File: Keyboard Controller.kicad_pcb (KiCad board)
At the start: 2 copper layers, 76.2 x 101.6 mm, 48 parts, among them SW1 SW_Push, SW2 SW_Push, SW3 SW_Push, SW4 SW_Push, SW5 SW_Push, SW6 SW_Push, SW7 SW_Push, SW8 SW_Push, SW9 SW_Push, U1 Teensy-3.2

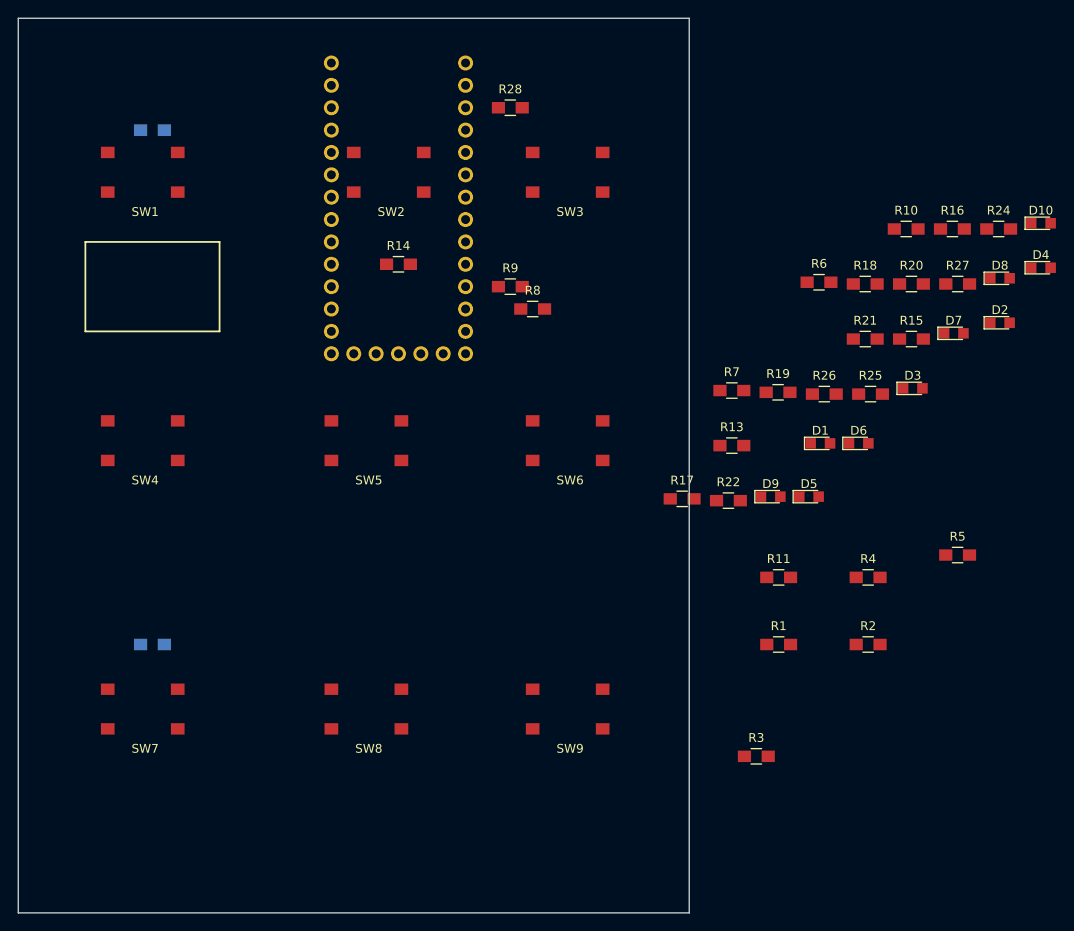
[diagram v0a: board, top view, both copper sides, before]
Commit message: Rough placement of all components except mounting holes
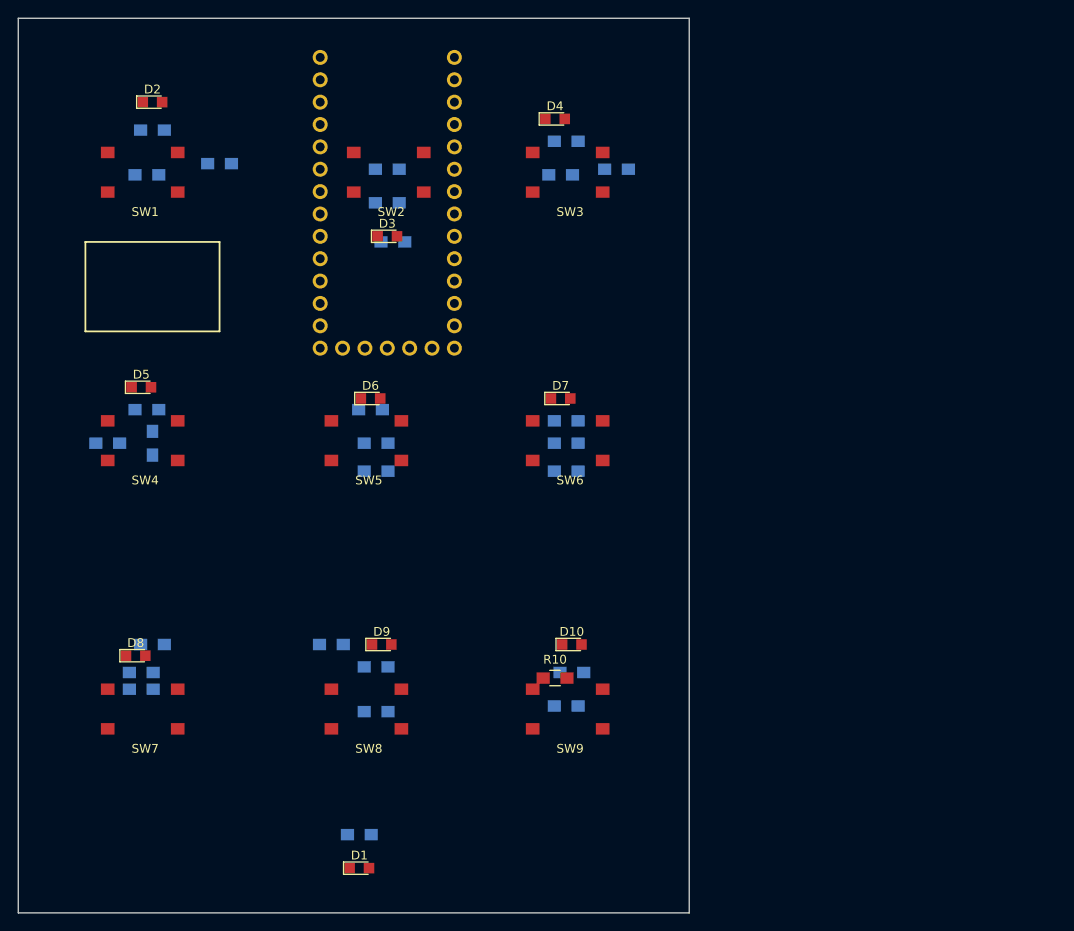
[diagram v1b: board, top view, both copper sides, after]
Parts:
- R1, R11, R13, R14, R15, R16, R17, R18, R19, R2, R20, R21, R22, R24, R25, R26, R27, R28, R3, R4, R5, R6, R7, R8, R9: moved to B.Cu
- moved R24 110.5 mm to (110.5, 116.8)
- moved D8 107.1 mm to (109.9, 113.0)
- moved D2 99.5 mm to (111.8, 50.2)
- moved R5 93.5 mm to (111.1, 85.1)
- moved R2 91.7 mm to (119.4, 57.1)
- moved R11 85.1 mm to (111.1, 58.4)
- moved R18 82.9 mm to (111.8, 88.9), turned to 270 degrees
- moved D5 76.8 mm to (110.5, 82.5)
- moved D10 71.6 mm to (159.4, 111.8)
- moved R3 71.5 mm to (139.1, 66.0)
- moved D1 71.2 mm to (135.3, 137.2)
- moved R25 66.7 mm to (137.2, 119.4)
- moved R17 65.5 mm to (106.7, 88.9)
- moved R27 65.4 mm to (158.8, 118.7)
- moved R10 64.7 mm to (157.5, 115.6)
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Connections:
- R10 pad 2: /LED8 -> /LED9
- R2 pad 2: /LED0 -> /LED1
- R3 pad 2: /LED1 -> /LED2
- R4 pad 2: /LED2 -> /LED3
- R5 pad 2: /LED3 -> /LED4
- R6 pad 2: /LED4 -> /LED5
- R7 pad 2: /LED5 -> /LED6
- R8 pad 2: /LED6 -> /LED7
- R9 pad 2: /LED7 -> /LED8
- U1 pad 10: /LED1 -> /LED2
- U1 pad 11: /LED2 -> /LED3
- U1 pad 12: /LED3 -> /LED4
- U1 pad 13: /LED4 -> /LED5
- U1 pad 14: /LED5 -> /LED6
- U1 pad 15: /LED6 -> /LED7
- U1 pad 16: /LED7 -> /LED8
- U1 pad 17: /LED8 -> /LED9
- U1 pad 9: /LED0 -> /LED1
